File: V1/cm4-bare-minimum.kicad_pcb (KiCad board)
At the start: 2 copper layers, 120 x 40 mm, 35 parts, among them J1 Conn_01x03, J2 Conn_01x03, J3 Micro_SD_Card_Det, J4 Molex 470531000, J5 THD-20-R, J6 USB_OTG, J7 USB4105-GF-A, J8 THD-02-R, U1 EMC2301-1-ACZL-TR, U2 RT9742GGJ5, U3 74LVC1G07SE-7, U4 FSUSB42MUX, U5 MagJack-A70-112-331N126

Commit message: Renamed V1 Requirements project
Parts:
- moved R9 97.3 mm to (66.7, 138.4), turned to 90 degrees
- moved U1 94.7 mm to (70.4, 137.6), turned to 0 degrees
- moved C2 89.6 mm to (67.1, 132.8), turned to -90 degrees
- moved U2 88.3 mm to (70.2, 132.8), turned to 0 degrees
- moved R10 87.2 mm to (72.8, 132.7), turned to -90 degrees
- moved C1 81.8 mm to (72.6, 128.7), turned to 0 degrees
- moved R5 81.0 mm to (59.3, 122.6), turned to 90 degrees
- moved R6 79.5 mm to (61.5, 122.6), turned to 90 degrees
- moved R4 78.6 mm to (59.3, 120.7), turned to 90 degrees
- moved R7 77.1 mm to (61.5, 120.7), turned to 90 degrees
- moved U3 75.0 mm to (60.3, 118.3), turned to 0 degrees
- moved R8 64.8 mm to (58.1, 107.9), turned to 90 degrees
- moved J5 58.8 mm to (151.7, 82.9), turned to -90 degrees
- moved R3 58.6 mm to (74.2, 112.1), turned to 0 degrees
- moved R2 57.8 mm to (76.1, 112.1), turned to 0 degrees
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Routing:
- net /GPIO21: track 31.2 -> 90.6 mm
- net /GPIO26: track 34.0 -> 88.8 mm
- net /GPIO20: track 34.5 -> 88.6 mm
- net /GPIO19: track 37.2 -> 86.9 mm
- net /GPIO16: track 37.8 -> 86.5 mm
- net /GPIO13: track 40.4 -> 84.8 mm
- net /GPIO6: track 43.6 -> 82.4 mm
- net /GPIO12: track 43.6 -> 81.7 mm
- net /GPIO2: track 87.5 -> 52.1 mm
- net /GPIO5: track 47.1 -> 80.5 mm
- net /GPIO3: track 84.3 -> 54.1 mm
- net /ID_SD: track 50.5 -> 78.6 mm
- net /ID_SC: track 49.5 -> 77.4 mm
- net /GPIO4: track 81.1 -> 56.2 mm
- net /USB_OTG_ID: track 23.9 -> 0.00 mm
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
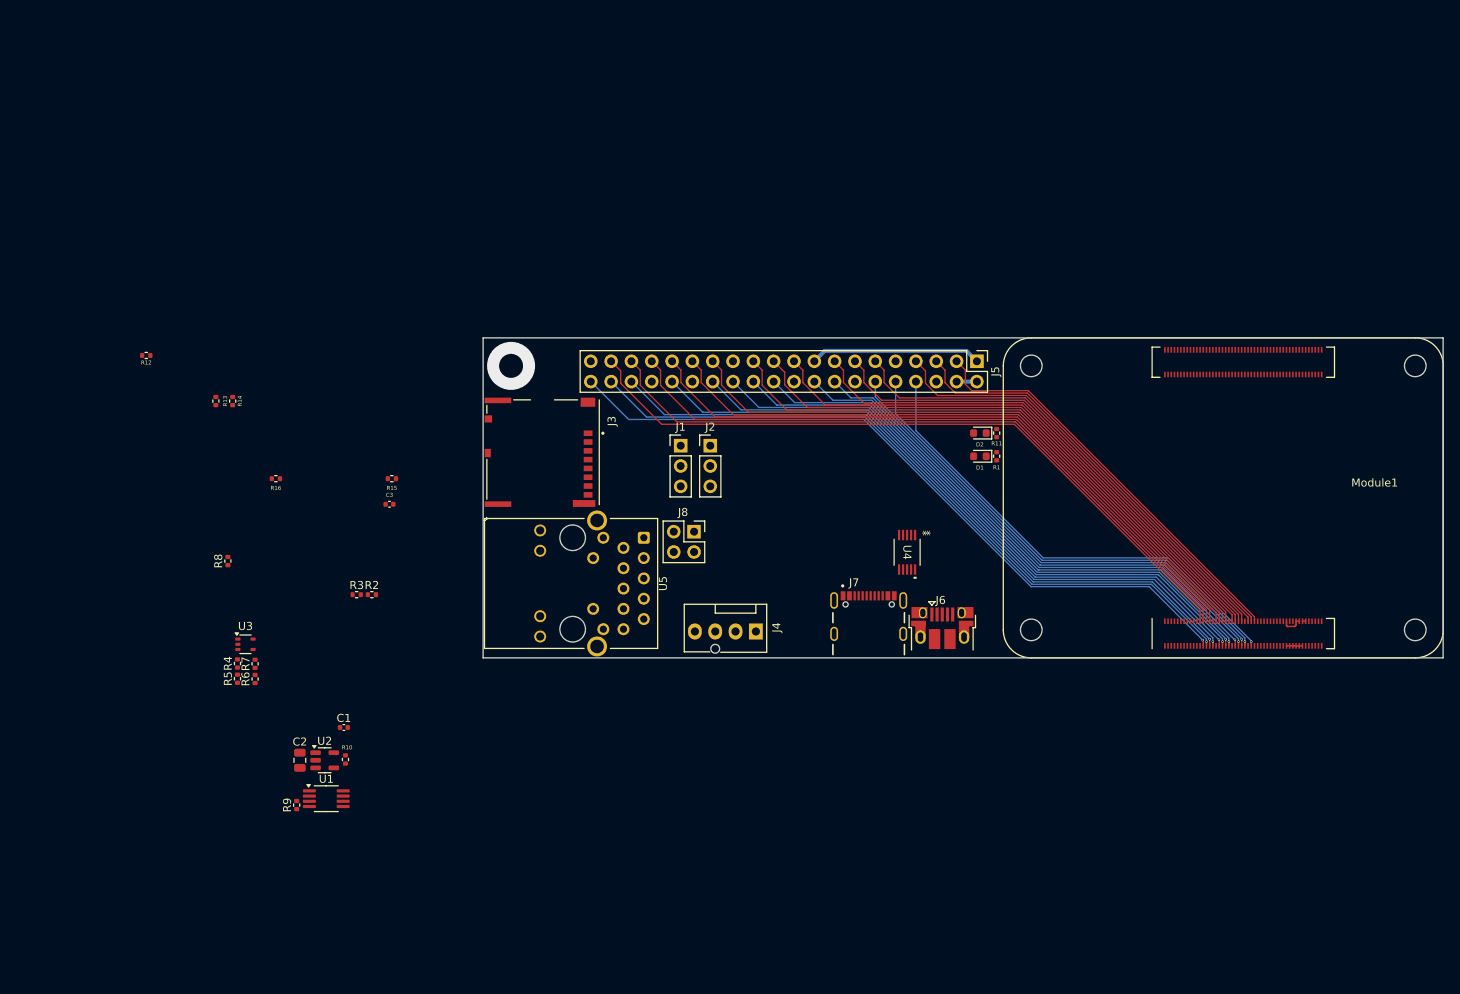
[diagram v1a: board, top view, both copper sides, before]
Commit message: PCB Layout Modified to Nano-ITX
Added M.2 connector, PSU, updated PCB layout for 120mm x 120mm. Connected GPIO header. Working on remaining component and tracks placement.
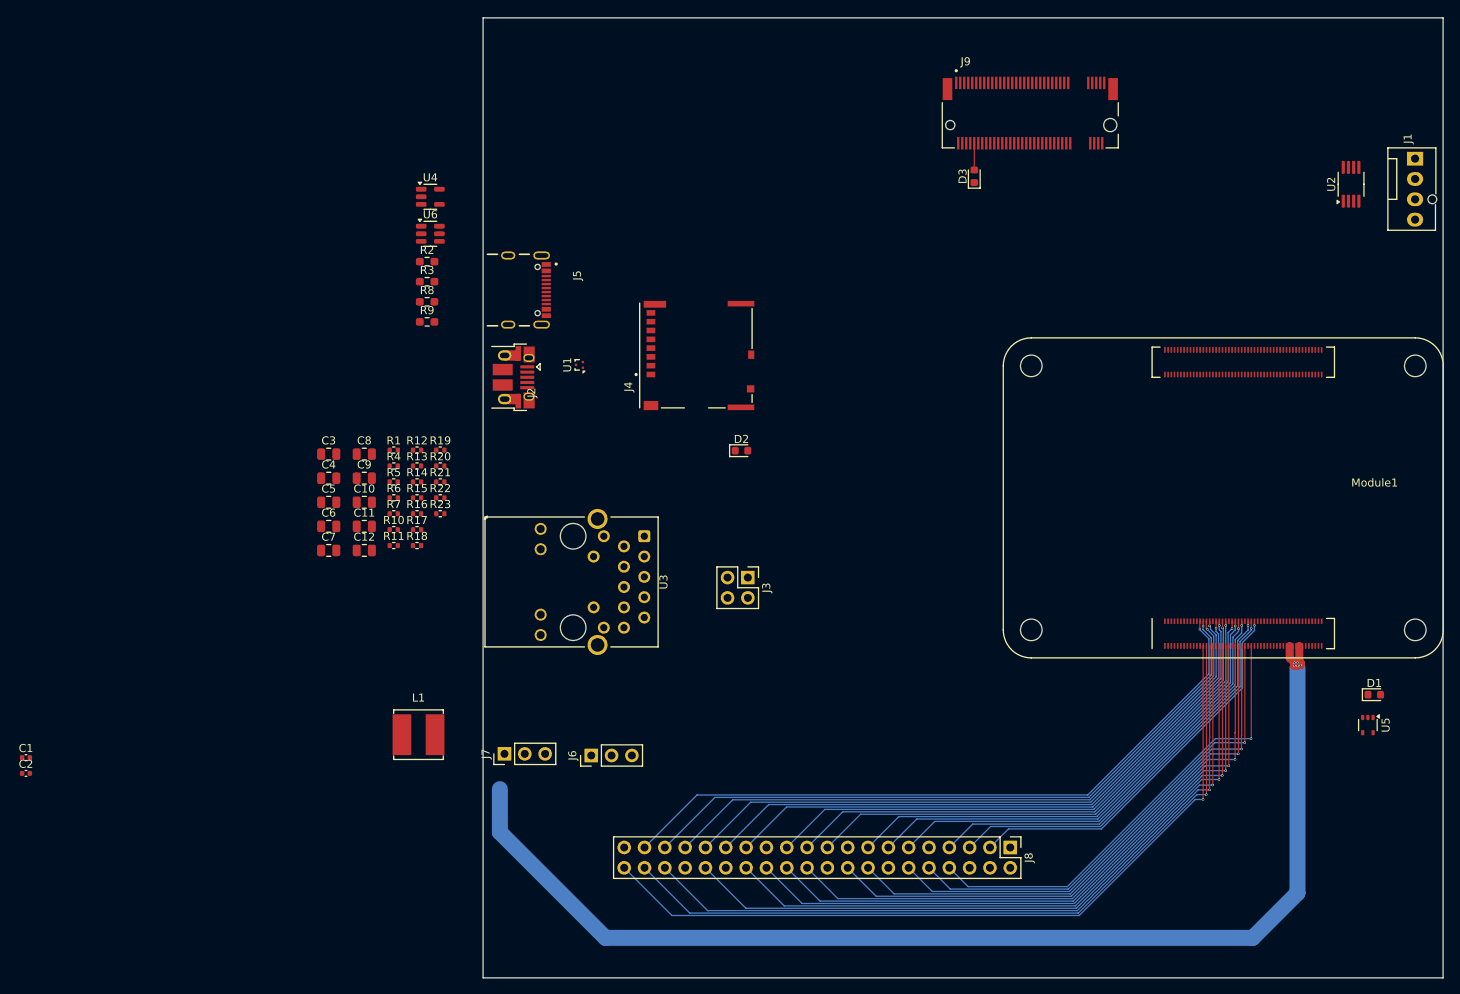
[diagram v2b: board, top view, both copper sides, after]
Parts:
- added C10: 10u, Capacitor_SMD:C_0805_2012Metric, F.Cu at (75.2, 100.5)
- added C11: 0.1u, Capacitor_SMD:C_0805_2012Metric, F.Cu at (75.2, 103.6)
- added C12: 10u, Capacitor_SMD:C_0805_2012Metric, F.Cu at (75.2, 106.6)
- added C4: 1u, Capacitor_SMD:C_0805_2012Metric, F.Cu at (70.7, 97.5)
- added C5: 13p, Capacitor_SMD:C_0805_2012Metric, F.Cu at (70.7, 100.5)
- added C6: 10u, Capacitor_SMD:C_0805_2012Metric, F.Cu at (70.7, 103.6)
- added C7: 0.1u, Capacitor_SMD:C_0805_2012Metric, F.Cu at (70.7, 106.6)
- added C8: 1u, Capacitor_SMD:C_0805_2012Metric, F.Cu at (75.2, 94.5)
- added C9: 10p, Capacitor_SMD:C_0805_2012Metric, F.Cu at (75.2, 97.5)
- added D3: LED Red, LED_SMD:LED_0603_1608Metric, F.Cu at (151.4, 59.8)
- added J9: MDT320M03001, MDT320M03001:AMPHENOL_MDT320M03001, F.Cu at (158.4, 53.4)
- added L1: SRN6045TA-4R7Y, Inductor_SMD:L_Bourns_SRN6045TA, F.Cu at (81.9, 129.6)
- added R17: NC, Resistor_SMD:R_0402_1005Metric, F.Cu at (81.7, 104.0)
- added R18: NC, Resistor_SMD:R_0402_1005Metric, F.Cu at (81.7, 106.0)
- added R19: 10, Resistor_SMD:R_0402_1005Metric, F.Cu at (84.7, 94.0)
- added R20: 40.2k, Resistor_SMD:R_0402_1005Metric, F.Cu at (84.7, 96.0)
- added R21: 100k, Resistor_SMD:R_0402_1005Metric, F.Cu at (84.7, 98.0)
- added R22: 20k, Resistor_SMD:R_0402_1005Metric, F.Cu at (84.7, 100.0)
- added R23: 13k, Resistor_SMD:R_0402_1005Metric, F.Cu at (84.7, 102.0)
- added U6: MP1470, Package_TO_SOT_SMD:TSOT-23-6, F.Cu at (83.4, 67.0)
- C2: value 10u -> 100n; footprint Capacitor_SMD:C_0805_2012Metric -> Capacitor_SMD:C_0402_1005Metric
- C3: value 100n -> 10u; footprint Capacitor_SMD:C_0402_1005Metric -> Capacitor_SMD:C_0805_2012Metric
- D1: value LED Green -> LED Red
- D2: value LED Red -> LED Green
- J1: value Conn_01x03 -> Molex 470531000; footprint Connector_PinHeader_2.54mm:PinHeader_1x03_P2.54mm_Vertical -> Connector:FanPinHeader_1x04_P2.54mm_Vertical
- J2: value Conn_01x03 -> USB_OTG; footprint Connector_PinHeader_2.54mm:PinHeader_1x03_P2.54mm_Vertical -> CM4IO:USB_Micro-B_EDAC_UCON00686
- J3: value Micro_SD_Card_Det -> THD-02-R; footprint CM4IO:SDCARD_MOLEX_503398-1892 -> Connector_PinHeader_2.54mm:PinHeader_2x02_P2.54mm_Vertical
- J4: value Molex 470531000 -> Micro_SD_Card_Det; footprint Connector:FanPinHeader_1x04_P2.54mm_Vertical -> CM4IO:SDCARD_MOLEX_503398-1892
- J5: value THD-20-R -> USB4105-GF-A; footprint Connector_PinHeader_2.54mm:PinHeader_2x20_P2.54mm_Vertical -> USB4105-GF-A:GCT_USB4105-GF-A
- J6: value USB_OTG -> Conn_01x03; footprint CM4IO:USB_Micro-B_EDAC_UCON00686 -> Connector_PinHeader_2.54mm:PinHeader_1x03_P2.54mm_Vertical
- J7: value USB4105-GF-A -> Conn_01x03; footprint USB4105-GF-A:GCT_USB4105-GF-A -> Connector_PinHeader_2.54mm:PinHeader_1x03_P2.54mm_Vertical
- J8: value THD-02-R -> THD-20-R; footprint Connector_PinHeader_2.54mm:PinHeader_2x02_P2.54mm_Vertical -> Connector_PinHeader_2.54mm:PinHeader_2x20_P2.54mm_Vertical
- R1: value 1k -> 36K 1%
- R11: value 1k -> NC
- R12: value 2.2K 1% -> 1k
- R13: value 5.1k -> 1k
- R14: value 5.1k -> NC
- R15: value 470R -> 1k
- R16: value 470R -> NC
- R2, R3: value NC -> 2.2K 1%; footprint Resistor_SMD:R_0402_1005Metric -> Resistor_SMD:R_0603_1608Metric_Pad0.98x0.95mm_HandSolder
- R4, R5: value NC -> 470R
- R8: value NC -> 5.1k; footprint Resistor_SMD:R_0402_1005Metric -> Resistor_SMD:R_0603_1608Metric_Pad0.98x0.95mm_HandSolder
- R9: value 36K 1% -> 5.1k; footprint Resistor_SMD:R_0402_1005Metric -> Resistor_SMD:R_0603_1608Metric_Pad0.98x0.95mm_HandSolder
- U1: value EMC2301-1-ACZL-TR -> TPD2EUSB30; footprint Package_SO:MSOP-8_3x3mm_P0.65mm -> Package_TO_SOT_SMD:Texas_DRT-3
- U2: value RT9742GGJ5 -> EMC2301-1-ACZL-TR; footprint Package_TO_SOT_SMD:SOT-23-5 -> Package_SO:MSOP-8_3x3mm_P0.65mm
- U3: value 74LVC1G07SE-7 -> MagJack-A70-112-331N126; footprint Package_TO_SOT_SMD:SOT-353_SC-70-5 -> CM4IO:TRJG0926HENL
- U4: value FSUSB42MUX -> RT9742GGJ5; footprint FSUSB42MUX:MSOP10_3X3_ONS -> Package_TO_SOT_SMD:SOT-23-5
- U5: value MagJack-A70-112-331N126 -> 74LVC1G07SE-7; footprint CM4IO:TRJG0926HENL -> Package_TO_SOT_SMD:SOT-353_SC-70-5
- moved U2 147.1 mm to (198.5, 60.8), turned to 90 degrees
- moved U5 101.0 mm to (200.6, 128.4)
- moved J1 98.6 mm to (206.5, 57.6), turned to -90 degrees
- moved R11 76.7 mm to (78.8, 106.0), turned to 0 degrees
- moved R1 75.4 mm to (78.8, 94.0), turned to 0 degrees
- moved U4 74.3 mm to (83.4, 62.4), turned to 0 degrees
- moved U1 62.8 mm to (102.0, 83.4), turned to 90 degrees
- moved R9 62.6 mm to (83.0, 78.0), turned to 0 degrees
- moved J5 59.3 mm to (93.1, 74.0)
- moved D1 57.6 mm to (201.4, 124.6), turned to 0 degrees
- moved J8 55.9 mm to (155.9, 143.7)
- moved J7 47.9 mm to (92.7, 132.0), turned to 90 degrees
- moved J6 46.3 mm to (103.5, 132.2), turned to 90 degrees
- moved R2 42.2 mm to (83.0, 70.5)
- moved U3 41.7 mm to (101.3, 110.5), turned to -90 degrees
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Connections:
- C2 pad 1: /SD_PWR -> Net-(C2-Pad1)
- C3 pad 1: Net-(C3-Pad1) -> /SD_PWR
- D1 pad 2: /CM4_3V3 -> /PWR_3V3
- D2 pad 2: /CM4_3V3 -> /PWR_3V3
- J1 pad 1: /Global_EN -> GND
- J1 pad 2: GND -> /CM4_5V
- J1 pad 3: /RUN_PG -> Net-(J1-Pin_3)
- J2 pad 1: Net-(J2-Pin_1) -> Net-(J2-VBUS)
- J2 pad 2: /nRPIBOOT -> /USB2_N
- J2 pad 3: GND -> /USB2_P
- J3 pad 1: /SD_DAT2 -> /TR1_TAP
- J3 pad 2: /SD_DAT3 -> /TR2_TAP
- J3 pad 3: /SD_CMD -> /TR0_TAP
- J3 pad 4: /SD_PWR -> /TR3_TAP
- J4 pad 1: GND -> /SD_DAT2
- J4 pad 2: /CM4_5V -> /SD_DAT3
- J4 pad 3: Net-(J4-Pin_3) -> /SD_CMD
- J4 pad 4: Net-(J4-Pin_4) -> /SD_PWR
- J6 pad 1: /USB_OTG_ID -> /Global_EN
- J6 pad 2: /USB_D_N -> GND
- J6 pad 3: /USB_D_P -> /RUN_PG
- J8 pad 1: /TR1_TAP -> /CM4_3V3
- J8 pad 2: /TR2_TAP -> /CM4_5V
- J8 pad 3: /TR0_TAP -> /GPIO2
- J8 pad 4: /TR3_TAP -> /CM4_5V
- Module1 pad 102: unconnected-(Module1B-PCIe_CLK_nREQ-Pad102) -> /PCIe_CLK_nREQ
- Module1 pad 109: unconnected-(Module1B-PCIe_nRST-Pad109) -> /PCIe_nRST
- Module1 pad 110: unconnected-(Module1B-PCIe_CLK_P-Pad110) -> /PCIe_CLK_P
- Module1 pad 112: unconnected-(Module1B-PCIe_CLK_N-Pad112) -> /PCIe_CLK_N
- Module1 pad 116: unconnected-(Module1B-PCIe_RX_P-Pad116) -> /PCIe_RX_P
- Module1 pad 118: unconnected-(Module1B-PCIe_RX_N-Pad118) -> /PCIe_RX_N
- Module1 pad 122: unconnected-(Module1B-PCIe_TX_P-Pad122) -> /PCIe_TX_P
- Module1 pad 124: unconnected-(Module1B-PCIe_TX_N-Pad124) -> /PCIe_TX_N
- Module1 pad 21: Net-(Module1A-PI_nLED_Activity) -> /PI_nLED_Activity
- Module1 pad 88: /CM4_1V8 -> unconnected-(Module1A-+1.8v_(Output)-Pad88)
- Module1 pad 90: /CM4_1V8 -> unconnected-(Module1A-+1.8v_(Output)-Pad90)
- R1 pad 1: Net-(D1-K) -> Net-(J1-Pin_3)
- R1 pad 2: Net-(Module1A-PI_nLED_Activity) -> /PWR_3V3
- R11 pad 1: Net-(D2-K) -> Net-(J7-Pin_1)
- R11 pad 2: Net-(R11-Pad2) -> /CM4_3V3
- R12 pad 1: /USB_OTG_ID -> /PWR_3V3
- R12 pad 2: GND -> /LED1
- R13 pad 1: /AnalogIP1 -> Net-(D1-K)
- R13 pad 2: GND -> Net-(R13-Pad2)
- R14 pad 1: /AnalogIP0 -> /SD_VDD_Override
- R15 pad 1: Net-(U5-LEDG_K) -> Net-(D2-K)
- R15 pad 2: /ETH_LEDG -> /PI_nLED_Activity
- R16 pad 1: Net-(U5-LEDY_K) -> /EEPROM_nWP
- R16 pad 2: /ETH_LEDY -> GND
- R2 pad 1: /CM4_3V3 -> Net-(J2-VBUS)
- R2 pad 2: Net-(J3-DET_A) -> /USB_OTG_ID
- R3 pad 1: /Reserved -> /USB_OTG_ID
- R3 pad 2: Net-(J3-DET_B) -> GND
- R4 pad 1: /SD_VDD_Override -> Net-(U3-LEDG_K)
- R4 pad 2: GND -> /ETH_LEDG
- R5 pad 1: /EEPROM_nWP -> Net-(U3-LEDY_K)
- R5 pad 2: GND -> /ETH_LEDY
- R6 pad 1: /BT_nDisable -> /CM4_3V3
- R6 pad 2: GND -> Net-(J4-DET_A)
- R7 pad 1: /WiFi_nDisable -> /Reserved
- R7 pad 2: GND -> Net-(J4-DET_B)
- R8 pad 1: Net-(J2-Pin_1) -> Net-(J5-CC1)
- R8 pad 2: /CM4_3V3 -> GND
- R9 pad 1: Net-(J4-Pin_3) -> Net-(J5-CC2)
- R9 pad 2: /CM4_3V3 -> GND
- U1 pad 1: /SDA0 -> /USB2_P
- U1 pad 2: /SCL0 -> /USB2_N
- U1 pad 3: /CM4_3V3 -> GND
- U2 pad 1: /SD_PWR -> /SDA0
- U2 pad 2: GND -> /SCL0
- U2 pad 3: unconnected-(U2-nFLG-Pad3) -> /CM4_3V3
- U2 pad 4: /SD_PWR_ON -> GND
- U2 pad 5: /CM4_3V3 -> Net-(J1-Pin_4)
- U3 pad 1: (no net) -> unconnected-(U3-TRD0+-Pad1)
- U3 pad 2: /nPI_LED_PWR -> /TRD0_N
- U3 pad 3: GND -> /TRD1_P
- U3 pad 4: Net-(R11-Pad2) -> Net-(C2-Pad1)
- U3 pad 5: /CM4_3V3 -> Net-(C2-Pad1)
- U4 pad 1: /CM4_3V3 -> /SD_PWR
- U4 pad 2: /USB_OTG_ID -> GND
- U4 pad 3: /USB2_P -> unconnected-(U4-nFLG-Pad3)
- U4 pad 4: /USB2_N -> /SD_PWR_ON
- U4 pad 5: GND -> /CM4_3V3
- U5 pad 1: unconnected-(U5-TRD0+-Pad1) -> (no net)
- U5 pad 2: /TRD0_N -> /nPI_LED_PWR
- U5 pad 3: /TRD1_P -> GND
- U5 pad 4: Net-(C3-Pad1) -> Net-(R13-Pad2)
- U5 pad 5: Net-(C3-Pad1) -> /CM4_3V3
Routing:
- net /CM4_5V: track 4.54 -> 147.7 mm, vias 0 -> 5
- net /CM4_3V3: track 24.1 -> 0.00 mm
- net /GPIO21: track 90.6 -> 100.0 mm
- net /GPIO20: track 88.6 -> 97.3 mm
- net /GPIO16: track 86.5 -> 94.6 mm
- net /GPIO12: track 81.7 -> 89.3 mm
- net /ID_SC: track 77.4 -> 84.3 mm
- net /GPIO7: track 75.4 -> 81.7 mm
- net /GPIO8: track 73.3 -> 78.9 mm
- net /GPIO25: track 71.2 -> 76.2 mm
- net /GPIO24: track 66.7 -> 71.2 mm
- net /GPIO23: track 64.7 -> 68.4 mm
- net /LED1: track 0.00 -> 3.34 mm
- net /GPIO2: track 52.1 -> 48.8 mm, vias 0 -> 1
- net /GPIO11: track 73.9 -> 70.6 mm, vias 0 -> 1
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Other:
- board size 120 x 40 mm -> 120 x 120 mm

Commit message: Updated V1 PCB Layout
Added Mounting Holes
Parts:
- added REF**: MountingHole_3.2mm_M3, MountingHole:MountingHole_3.2mm_M3, F.Cu at (95.0, 155.0)
- added REF**: MountingHole_3.2mm_M3, MountingHole:MountingHole_3.2mm_M3, F.Cu at (205.0, 155.0)
- added REF**: MountingHole_3.2mm_M3, MountingHole:MountingHole_3.2mm_M3, F.Cu at (205.0, 45.0)
- added REF**: MountingHole_3.2mm_M3, MountingHole:MountingHole_3.2mm_M3, F.Cu at (95.0, 45.0)
- moved J7 9.89 mm to (102.0, 128.7)
- moved J6 9.89 mm to (112.8, 128.9)
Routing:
- net /CM4_3V3: track 0.00 -> 21.4 mm
- net /CM4_5V: track 147.7 -> 165.2 mm, vias 5 -> 7
